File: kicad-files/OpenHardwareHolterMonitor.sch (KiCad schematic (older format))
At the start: 30 parts, among them CON1 Micro_SD_Card, J1 Conn_02x06_Odd_Even, P1 Custom_FTDI, Q1 S8050, Q2 S8050, Q3 Q_NMOS_DGS, Q4 Q_NMOS_DGS, U1 ESP-WROOM-32, Y1 32768Hz

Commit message: continue assigning part numbers for BOM
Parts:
- C1, C2: ManufacturerName (none) -> Yageo; manufacturer-pn C0603C120J5GAC -> CC0603JRNPO9BN120
- CON1: ManufacturerName (none) -> Wurth; manufacturer-pn (none) -> 693072010801
- J1: symbol Connector:Conn_02x06_Odd_Even -> OpenHardwareHolterMonitor-rescue:Conn_02x06_Odd_Even-Connector
- MH_NE1, MH_NW1, MH_SE1, MH_SW1: symbol Mechanical:Mounting_Hole -> OpenHardwareHolterMonitor-rescue:Mounting_Hole-Mechanical
- TP1, TP2, TP3: symbol Connector:Test_Point -> OpenHardwareHolterMonitor-rescue:Test_Point-Connector
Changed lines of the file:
@@
 F 2 "Connectors_Card:MicroSd_Wurth_693072010801" H 3650 5900 50  0001 C CNN
 F 3 "" H 2500 5600 50  0000 C CNN
+F 4 "Wurth" H 0   0   50  0001 C CNN "ManufacturerName"
+F 5 "693072010801" H 0   0   50  0001 C CNN "manufacturer-pn"
 	1    2500 5600
 	0    1    1    0
@@
 F 2 "Capacitors_SMD:C_0603_HandSoldering" H 7988 2600 50  0001 C CNN
 F 3 "" H 7950 2750 50  0000 C CNN
-F 4 "C0603C120J5GAC" H 0   0   50  0001 C CNN "manufacturer-pn"
+F 4 "CC0603JRNPO9BN120 " H 0   0   50  0001 C CNN "manufacturer-pn"
+F 5 "Yageo" H 0   0   50  0001 C CNN "ManufacturerName"
 	1    7950 2750
 	1    0    0    -1
@@
 F 2 "Capacitors_SMD:C_0603_HandSoldering" H 8588 2600 50  0001 C CNN
 F 3 "" H 8550 2750 50  0000 C CNN
-F 4 "C0603C120J5GAC" H 0   0   50  0001 C CNN "manufacturer-pn"
+F 4 "CC0603JRNPO9BN120 " H 0   0   50  0001 C CNN "manufacturer-pn"
+F 5 "Yageo" H 0   0   50  0001 C CNN "ManufacturerName"
 	1    8550 2750
 	1    0    0    -1
@@
 	9550 5600 10200 5600
 $Comp
-L Connector:Test_Point TP1
+L OpenHardwareHolterMonitor-rescue:Test_Point-Connector TP1
 U 1 1 5C99AAF0
 P 10200 5600
@@
 $EndComp
 $Comp
-L Connector:Test_Point TP2
+L OpenHardwareHolterMonitor-rescue:Test_Point-Connector TP2
 U 1 1 5C99ABBF
 P 10200 5800
@@
 $EndComp
 $Comp
-L Connector:Test_Point TP3
+L OpenHardwareHolterMonitor-rescue:Test_Point-Connector TP3
 U 1 1 5C99AC98
 P 10200 6000
@@
 $EndComp
 $Comp
-L Connector:Conn_02x06_Odd_Even J1
+L OpenHardwareHolterMonitor-rescue:Conn_02x06_Odd_Even-Connector J1
 U 1 1 5CAE7D82
 P 10400 2300
@@
 	1350 1900 900  1900
 $Comp
-L Mechanical:Mounting_Hole MH_NW1
+L OpenHardwareHolterMonitor-rescue:Mounting_Hole-Mechanical MH_NW1
 U 1 1 5C1F5248
 P 850 7150
@@
 $EndComp
 $Comp
-L Mechanical:Mounting_Hole MH_SW1
+L OpenHardwareHolterMonitor-rescue:Mounting_Hole-Mechanical MH_SW1
 U 1 1 5C1F5695
 P 850 7450
@@
 $EndComp
 $Comp
-L Mechanical:Mounting_Hole MH_NE1
+L OpenHardwareHolterMonitor-rescue:Mounting_Hole-Mechanical MH_NE1
 U 1 1 5C1F5739
 P 2000 7150
@@
 $EndComp
 $Comp
-L Mechanical:Mounting_Hole MH_SE1
+L OpenHardwareHolterMonitor-rescue:Mounting_Hole-Mechanical MH_SE1
 U 1 1 5C1F57DC
 P 2000 7450

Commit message: someone set us up the BoM
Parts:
- J1: ManufacturerName (none) -> Harwin; manufacturer-pn (none) -> M50-3000645
- P1: ManufacturerName (none) -> Wurth; manufacturer-pn (none) -> 61300711121
- Q1, Q2: ManufacturerName (none) -> Diodes Incorporated; manufacturer-pn (none) -> DSS4240T-7
- Q3, Q4: ManufacturerName (none) -> Diodes Incorporated; manufacturer-pn (none) -> 2N7002-7-F
- R1, R2, R3, R4: ManufacturerName (none) -> Panasonic Electronic Components; manufacturer-pn (none) -> ERA-3AEB470V
- R10, R7: ManufacturerName (none) -> Panasonic Electronic Components; manufacturer-pn (none) -> ERA-3AEB104V
- R11, R8: ManufacturerName (none) -> Panasonic Electronic Components; manufacturer-pn (none) -> ERJ-PB3B3901V
- R12, R9: ManufacturerName (none) -> Panasonic Electronic Components; manufacturer-pn (none) -> ERJ-PB3B1001V
- R5, R6: ManufacturerName (none) -> Panasonic Electronic Components; manufacturer-pn (none) -> ERJ-PB3B1202V
- U1: ManufacturerName (none) -> RF Solutions; manufacturer-pn (none) -> ESP-32
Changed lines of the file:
@@
 F 2 "esp-wroom-32:MODULE_ESP-WROOM-32" H 2550 2550 60  0001 C CNN
 F 3 "" H 2550 2550 60  0001 C CNN
+F 4 " RF Solutions" H 0   0   50  0001 C CNN "ManufacturerName"
+F 5 "ESP-32" H 0   0   50  0001 C CNN "manufacturer-pn"
 	1    2550 2550
 	1    0    0    -1
@@
 F 2 "TO_SOT_Packages_SMD:SOT-23_Handsoldering" H 4900 4975 50  0000 L CIN
 F 3 "" H 4700 5050 50  0000 L CNN
+F 4 "Diodes Incorporated" H 0   0   50  0001 C CNN "ManufacturerName"
+F 5 "DSS4240T-7" H 0   0   50  0001 C CNN "manufacturer-pn"
 	1    4700 5050
 	1    0    0    -1
@@
 F 2 "TO_SOT_Packages_SMD:SOT-23_Handsoldering" H 4900 5725 50  0000 L CIN
 F 3 "" H 4700 5800 50  0000 L CNN
+F 4 "Diodes Incorporated" H 0   0   50  0001 C CNN "ManufacturerName"
+F 5 "DSS4240T-7" H 0   0   50  0001 C CNN "manufacturer-pn"
 	1    4700 5800
 	1    0    0    1
@@
 F 2 "Resistors_SMD:R_0603_HandSoldering" V 4180 5050 50  0001 C CNN
 F 3 "" H 4250 5050 50  0000 C CNN
+F 4 "Panasonic Electronic Components" H 0   0   50  0001 C CNN "ManufacturerName"
+F 5 "ERJ-PB3B1202V" H 0   0   50  0001 C CNN "manufacturer-pn"
 	1    4250 5050
 	0    1    1    0
@@
 F 2 "Resistors_SMD:R_0603_HandSoldering" V 4180 5800 50  0001 C CNN
 F 3 "" H 4250 5800 50  0000 C CNN
+F 4 "Panasonic Electronic Components" H 0   0   50  0001 C CNN "ManufacturerName"
+F 5 "ERJ-PB3B1202V" H 0   0   50  0001 C CNN "manufacturer-pn"
 	1    4250 5800
 	0    1    1    0
@@
 F 2 "Pin_Headers:Pin_Header_Straight_1x07_Pitch2.54mm" H 5300 6650 50  0001 C CNN
 F 3 "" H 5300 6650 50  0000 C CNN
+F 4 "Wurth" H 0   0   50  0001 C CNN "ManufacturerName"
+F 5 "61300711121" H 0   0   50  0001 C CNN "manufacturer-pn"
 	1    5300 6650
 	1    0    0    -1
@@
 F 2 "Resistors_SMD:R_0603_HandSoldering" V 4280 2000 50  0001 C CNN
 F 3 "" H 4350 2000 50  0000 C CNN
+F 4 "Panasonic Electronic Components" H 0   0   50  0001 C CNN "ManufacturerName"
+F 5 "ERA-3AEB470V" H 0   0   50  0001 C CNN "manufacturer-pn"
 	1    4350 2000
 	0    1    1    0
@@
 F 2 "Resistors_SMD:R_0603_HandSoldering" V 4280 2700 50  0001 C CNN
 F 3 "" H 4350 2700 50  0000 C CNN
+F 4 "Panasonic Electronic Components" H 0   0   50  0001 C CNN "ManufacturerName"
+F 5 "ERA-3AEB470V" H 0   0   50  0001 C CNN "manufacturer-pn"
 	1    4350 2700
 	0    1    1    0
@@
 F 2 "Resistors_SMD:R_0603_HandSoldering" V 4280 2800 50  0001 C CNN
 F 3 "" H 4350 2800 50  0000 C CNN
+F 4 "Panasonic Electronic Components" H 0   0   50  0001 C CNN "ManufacturerName"
+F 5 "ERA-3AEB470V" H 0   0   50  0001 C CNN "manufacturer-pn"
 	1    4350 2800
 	0    1    1    0
@@
 F 2 "Resistors_SMD:R_0603_HandSoldering" V 4280 2900 50  0001 C CNN
 F 3 "" H 4350 2900 50  0000 C CNN
+F 4 "Panasonic Electronic Components" H 0   0   50  0001 C CNN "ManufacturerName"
+F 5 "ERA-3AEB470V" H 0   0   50  0001 C CNN "manufacturer-pn"
 	1    4350 2900
 	0    1    1    0
@@
 F 2 "Resistors_SMD:R_0603_HandSoldering" V 8380 3950 50  0001 C CNN
 F 3 "" H 8450 3950 50  0000 C CNN
+F 4 "Panasonic Electronic Components" H 0   0   50  0001 C CNN "ManufacturerName"
+F 5 "ERJ-PB3B3901V" H 0   0   50  0001 C CNN "manufacturer-pn"
 	1    8450 3950
 	1    0    0    -1
@@
 F 2 "Resistors_SMD:R_0603_HandSoldering" V 8380 4400 50  0001 C CNN
 F 3 "" H 8450 4400 50  0000 C CNN
+F 4 "Panasonic Electronic Components" H 0   0   50  0001 C CNN "ManufacturerName"
+F 5 "ERJ-PB3B1001V" H 0   0   50  0001 C CNN "manufacturer-pn"
 	1    8450 4400
 	1    0    0    -1
@@
 F 2 "TO_SOT_Packages_SMD:SOT-23W_Handsoldering" H 8550 4900 50  0001 C CNN
 F 3 "" H 8350 4800 50  0000 C CNN
+F 4 "Diodes Incorporated" H 0   0   50  0001 C CNN "ManufacturerName"
+F 5 "2N7002-7-F " H 0   0   50  0001 C CNN "manufacturer-pn"
 	1    8350 4800
 	1    0    0    -1
@@
 F 2 "Resistors_SMD:R_0603_HandSoldering" V 10130 3950 50  0001 C CNN
 F 3 "" H 10200 3950 50  0000 C CNN
+F 4 "Panasonic Electronic Components" H 0   0   50  0001 C CNN "ManufacturerName"
+F 5 "ERJ-PB3B3901V" H 0   0   50  0001 C CNN "manufacturer-pn"
 	1    10200 3950
 	1    0    0    -1
@@
 F 2 "Resistors_SMD:R_0603_HandSoldering" V 10130 4400 50  0001 C CNN
 F 3 "" H 10200 4400 50  0000 C CNN
+F 4 "Panasonic Electronic Components" H 0   0   50  0001 C CNN "ManufacturerName"
+F 5 "ERJ-PB3B1001V" H 0   0   50  0001 C CNN "manufacturer-pn"
 	1    10200 4400
 	1    0    0    -1
@@
 F 2 "TO_SOT_Packages_SMD:SOT-23W_Handsoldering" H 10300 4900 50  0001 C CNN
 F 3 "" H 10100 4800 50  0000 C CNN
+F 4 "Diodes Incorporated" H 0   0   50  0001 C CNN "ManufacturerName"
+F 5 "2N7002-7-F " H 0   0   50  0001 C CNN "manufacturer-pn"
 	1    10100 4800
 	1    0    0    -1
@@
 F 2 "Resistors_SMD:R_0603_HandSoldering" V 9580 5000 50  0001 C CNN
 F 3 "" H 9650 5000 50  0000 C CNN
+F 4 "Panasonic Electronic Components" H 0   0   50  0001 C CNN "ManufacturerName"
+F 5 "ERA-3AEB104V" H 0   0   50  0001 C CNN "manufacturer-pn"
 	1    9650 5000
 	1    0    0    -1
@@
 F 2 "Resistors_SMD:R_0603_HandSoldering" V 7830 5000 50  0001 C CNN
 F 3 "" H 7900 5000 50  0000 C CNN
+F 4 "Panasonic Electronic Components" H 0   0   50  0001 C CNN "ManufacturerName"
+F 5 "ERA-3AEB104V" H 0   0   50  0001 C CNN "manufacturer-pn"
 	1    7900 5000
 	1    0    0    -1
@@
 F 2 "Pin_Headers:Pin_Header_Straight_2x06_Pitch1.27mm" H 10400 2300 50  0001 C CNN
 F 3 "~" H 10400 2300 50  0001 C CNN
+F 4 "Harwin" H 0   0   50  0001 C CNN "ManufacturerName"
+F 5 "M50-3000645" H 0   0   50  0001 C CNN "manufacturer-pn"
 	1    10400 2300
 	1    0    0    -1

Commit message: checked BoM
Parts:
- Y1: ManufacturerName (none) -> Fox
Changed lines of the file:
@@
 F 3 "" H 8250 2300 50  0000 C CNN
 F 4 "FK161EIHM0.032768" H 8250 2150 50  0000 C CNN "manufacturer-pn"
+F 5 "Fox" H 0   0   50  0001 C CNN "ManufacturerName"
 	1    8250 2300
 	1    0    0    -1

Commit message: fix schematic to use standard transistor pin numbers
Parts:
- Q1, Q2: symbol OpenHardwareHolterMonitor-rescue:S8050 -> Device:Q_NPN_BEC
- Q3, Q4: value Q_NMOS_DGS -> 2N7002; symbol OpenHardwareHolterMonitor-rescue:Q_NMOS_DGS -> Device:Q_NMOS_GSD
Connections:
- net DTR: now also Q2.2 (E); no longer Q2.1 (E)
- net Enable_vbat_read: now also Q3.1 (G), Q4.1 (G); no longer Q3.2 (G), Q4.2 (G)
- net GND: now also Q3.2 (S), Q4.2 (S); no longer Q3.3 (S), Q4.3 (S)
- net RTS: now also Q1.2 (E); no longer Q1.1 (E)
- net at R5.1: now also Q1.1 (B); no longer Q1.2 (B)
- net at R6.1: now also Q2.1 (B); no longer Q2.2 (B)
- net at R9.2: now also Q3.3 (D); no longer Q3.1 (D)
- net at R12.2: now also Q4.3 (D); no longer Q4.1 (D)
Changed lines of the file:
@@
 $EndComp
 $Comp
-L OpenHardwareHolterMonitor-rescue:S8050 Q1
+L Device:Q_NPN_BEC Q1
 U 1 1 5A2C0790
 P 4700 5050
@@
 $EndComp
 $Comp
-L OpenHardwareHolterMonitor-rescue:S8050 Q2
+L Device:Q_NPN_BEC Q2
 U 1 1 5A2C0855
 P 4700 5800
@@
 	8450 3750 8450 3800
 $Comp
-L OpenHardwareHolterMonitor-rescue:Q_NMOS_DGS Q3
+L Device:Q_NMOS_GSD Q3
 U 1 1 5AB6876E
 P 8350 4800
 F 0 "Q3" H 8550 4850 50  0000 L CNN
-F 1 "Q_NMOS_DGS" H 8550 4750 50  0000 L CNN
+F 1 "2N7002" H 8550 4750 50  0000 L CNN
 F 2 "TO_SOT_Packages_SMD:SOT-23W_Handsoldering" H 8550 4900 50  0001 C CNN
 F 3 "" H 8350 4800 50  0000 C CNN
@@
 	10200 3750 10200 3800
 $Comp
-L OpenHardwareHolterMonitor-rescue:Q_NMOS_DGS Q4
+L Device:Q_NMOS_GSD Q4
 U 1 1 5AB6D189
 P 10100 4800
 F 0 "Q4" H 10300 4850 50  0000 L CNN
-F 1 "Q_NMOS_DGS" H 10300 4750 50  0000 L CNN
+F 1 "2N7002" H 10300 4750 50  0000 L CNN
 F 2 "TO_SOT_Packages_SMD:SOT-23W_Handsoldering" H 10300 4900 50  0001 C CNN
 F 3 "" H 10100 4800 50  0000 C CNN

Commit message: switch to consistent SOT-23 footprint
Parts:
- Q3, Q4: footprint TO_SOT_Packages_SMD:SOT-23W_Handsoldering -> TO_SOT_Packages_SMD:SOT-23_Handsoldering
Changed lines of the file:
@@
 F 0 "Q3" H 8550 4850 50  0000 L CNN
 F 1 "2N7002" H 8550 4750 50  0000 L CNN
-F 2 "TO_SOT_Packages_SMD:SOT-23W_Handsoldering" H 8550 4900 50  0001 C CNN
+F 2 "TO_SOT_Packages_SMD:SOT-23_Handsoldering" H 8550 4900 50  0001 C CNN
 F 3 "" H 8350 4800 50  0000 C CNN
 F 4 "Diodes Incorporated" H 0   0   50  0001 C CNN "ManufacturerName"
@@
 F 0 "Q4" H 10300 4850 50  0000 L CNN
 F 1 "2N7002" H 10300 4750 50  0000 L CNN
-F 2 "TO_SOT_Packages_SMD:SOT-23W_Handsoldering" H 10300 4900 50  0001 C CNN
+F 2 "TO_SOT_Packages_SMD:SOT-23_Handsoldering" H 10300 4900 50  0001 C CNN
 F 3 "" H 10100 4800 50  0000 C CNN
 F 4 "Diodes Incorporated" H 0   0   50  0001 C CNN "ManufacturerName"

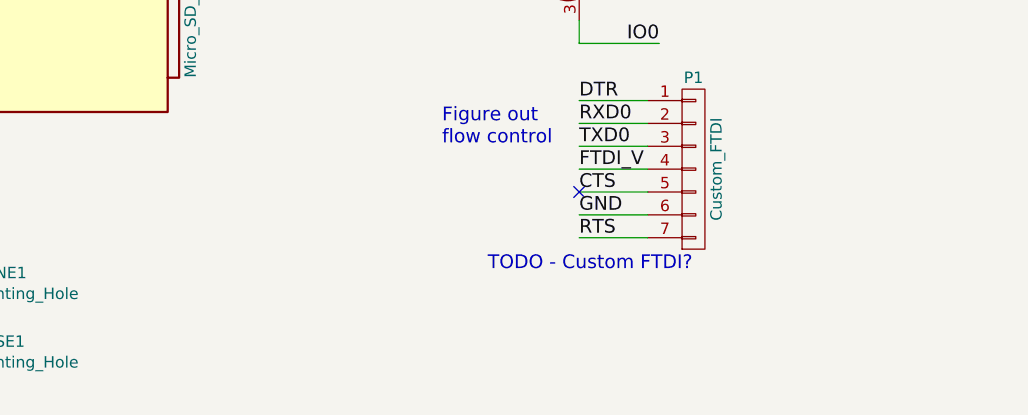
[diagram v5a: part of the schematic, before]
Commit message: Align Fiducials and Logo on schematic and PCB
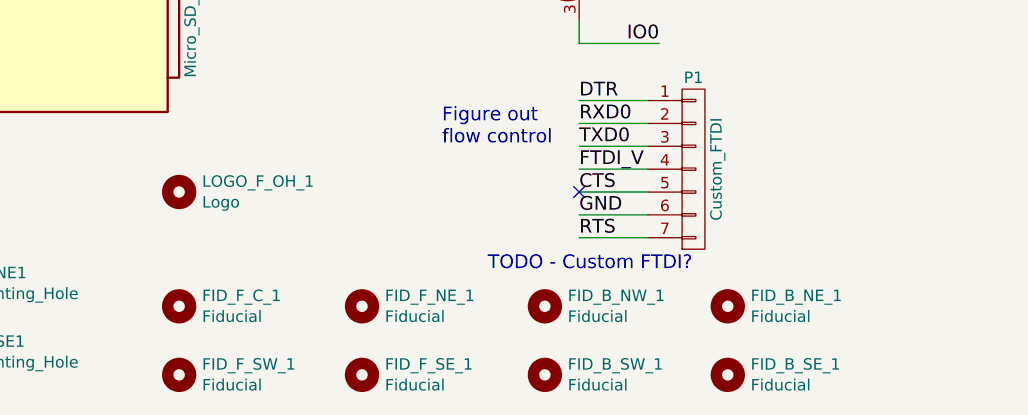
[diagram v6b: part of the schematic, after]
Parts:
- added FID_B_NE_1, FID_B_NW_1, FID_B_SE_1, FID_B_SW_1, FID_F_C_1, FID_F_NE_1, FID_F_SE_1, FID_F_SW_1: Fiducial, Fiducial:Fiducial_1mm_Dia_2.54mm_Outer_CopperTop, symbol OpenHardwareHolterMonitor-rescue:Mounting_Hole-Mechanical
- added LOGO_F_OH_1: Logo, Symbol:OSHW-Logo2_9.8x8mm_SilkScreen, symbol OpenHardwareHolterMonitor-rescue:Mounting_Hole-Mechanical
- R1, R10, R11, R12, R2, R3, R4, R5, R6, R7, R8, R9: footprint Resistors_SMD:R_0603_HandSoldering -> Resistor_SMD:R_0603_1608Metric_Pad1.05x0.95mm_HandSolder
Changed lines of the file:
@@
 F 0 "R5" V 4330 5050 50  0000 C CNN
 F 1 "12K" V 4250 5050 50  0000 C CNN
-F 2 "Resistors_SMD:R_0603_HandSoldering" V 4180 5050 50  0001 C CNN
+F 2 "Resistor_SMD:R_0603_1608Metric_Pad1.05x0.95mm_HandSolder" V 4180 5050 50  0001 C CNN
 F 3 "" H 4250 5050 50  0000 C CNN
 F 4 "Panasonic Electronic Components" H 0   0   50  0001 C CNN "ManufacturerName"
@@
 F 0 "R6" V 4330 5800 50  0000 C CNN
 F 1 "12K" V 4250 5800 50  0000 C CNN
-F 2 "Resistors_SMD:R_0603_HandSoldering" V 4180 5800 50  0001 C CNN
+F 2 "Resistor_SMD:R_0603_1608Metric_Pad1.05x0.95mm_HandSolder" V 4180 5800 50  0001 C CNN
 F 3 "" H 4250 5800 50  0000 C CNN
 F 4 "Panasonic Electronic Components" H 0   0   50  0001 C CNN "ManufacturerName"
@@
 F 0 "R1" V 4430 2000 50  0000 C CNN
 F 1 "47" V 4350 2000 50  0000 C CNN
-F 2 "Resistors_SMD:R_0603_HandSoldering" V 4280 2000 50  0001 C CNN
+F 2 "Resistor_SMD:R_0603_1608Metric_Pad1.05x0.95mm_HandSolder" V 4280 2000 50  0001 C CNN
 F 3 "" H 4350 2000 50  0000 C CNN
 F 4 "Panasonic Electronic Components" H 0   0   50  0001 C CNN "ManufacturerName"
@@
 F 0 "R2" V 4430 2700 50  0000 C CNN
 F 1 "47" V 4350 2700 50  0000 C CNN
-F 2 "Resistors_SMD:R_0603_HandSoldering" V 4280 2700 50  0001 C CNN
+F 2 "Resistor_SMD:R_0603_1608Metric_Pad1.05x0.95mm_HandSolder" V 4280 2700 50  0001 C CNN
 F 3 "" H 4350 2700 50  0000 C CNN
 F 4 "Panasonic Electronic Components" H 0   0   50  0001 C CNN "ManufacturerName"
@@
 F 0 "R3" V 4430 2800 50  0000 C CNN
 F 1 "47" V 4350 2800 50  0000 C CNN
-F 2 "Resistors_SMD:R_0603_HandSoldering" V 4280 2800 50  0001 C CNN
+F 2 "Resistor_SMD:R_0603_1608Metric_Pad1.05x0.95mm_HandSolder" V 4280 2800 50  0001 C CNN
 F 3 "" H 4350 2800 50  0000 C CNN
 F 4 "Panasonic Electronic Components" H 0   0   50  0001 C CNN "ManufacturerName"
@@
 F 0 "R4" V 4430 2900 50  0000 C CNN
 F 1 "47" V 4350 2900 50  0000 C CNN
-F 2 "Resistors_SMD:R_0603_HandSoldering" V 4280 2900 50  0001 C CNN
+F 2 "Resistor_SMD:R_0603_1608Metric_Pad1.05x0.95mm_HandSolder" V 4280 2900 50  0001 C CNN
 F 3 "" H 4350 2900 50  0000 C CNN
 F 4 "Panasonic Electronic Components" H 0   0   50  0001 C CNN "ManufacturerName"
@@
 F 0 "R8" V 8530 3950 50  0000 C CNN
 F 1 "3.9k" V 8450 3950 50  0000 C CNN
-F 2 "Resistors_SMD:R_0603_HandSoldering" V 8380 3950 50  0001 C CNN
+F 2 "Resistor_SMD:R_0603_1608Metric_Pad1.05x0.95mm_HandSolder" V 8380 3950 50  0001 C CNN
 F 3 "" H 8450 3950 50  0000 C CNN
 F 4 "Panasonic Electronic Components" H 0   0   50  0001 C CNN "ManufacturerName"
@@
 F 0 "R9" V 8530 4400 50  0000 C CNN
 F 1 "1k" V 8450 4400 50  0000 C CNN
-F 2 "Resistors_SMD:R_0603_HandSoldering" V 8380 4400 50  0001 C CNN
+F 2 "Resistor_SMD:R_0603_1608Metric_Pad1.05x0.95mm_HandSolder" V 8380 4400 50  0001 C CNN
 F 3 "" H 8450 4400 50  0000 C CNN
 F 4 "Panasonic Electronic Components" H 0   0   50  0001 C CNN "ManufacturerName"
@@
 F 0 "R11" V 10280 3950 50  0000 C CNN
 F 1 "3.9k" V 10200 3950 50  0000 C CNN
-F 2 "Resistors_SMD:R_0603_HandSoldering" V 10130 3950 50  0001 C CNN
+F 2 "Resistor_SMD:R_0603_1608Metric_Pad1.05x0.95mm_HandSolder" V 10130 3950 50  0001 C CNN
 F 3 "" H 10200 3950 50  0000 C CNN
 F 4 "Panasonic Electronic Components" H 0   0   50  0001 C CNN "ManufacturerName"
@@
 F 0 "R12" V 10280 4400 50  0000 C CNN
 F 1 "1k" V 10200 4400 50  0000 C CNN
-F 2 "Resistors_SMD:R_0603_HandSoldering" V 10130 4400 50  0001 C CNN
+F 2 "Resistor_SMD:R_0603_1608Metric_Pad1.05x0.95mm_HandSolder" V 10130 4400 50  0001 C CNN
 F 3 "" H 10200 4400 50  0000 C CNN
 F 4 "Panasonic Electronic Components" H 0   0   50  0001 C CNN "ManufacturerName"
@@
 F 0 "R10" V 9730 5000 50  0000 C CNN
 F 1 "100k" V 9650 5000 50  0000 C CNN
-F 2 "Resistors_SMD:R_0603_HandSoldering" V 9580 5000 50  0001 C CNN
+F 2 "Resistor_SMD:R_0603_1608Metric_Pad1.05x0.95mm_HandSolder" V 9580 5000 50  0001 C CNN
 F 3 "" H 9650 5000 50  0000 C CNN
 F 4 "Panasonic Electronic Components" H 0   0   50  0001 C CNN "ManufacturerName"
@@
 F 0 "R7" V 7980 5000 50  0000 C CNN
 F 1 "100k" V 7900 5000 50  0000 C CNN
-F 2 "Resistors_SMD:R_0603_HandSoldering" V 7830 5000 50  0001 C CNN
+F 2 "Resistor_SMD:R_0603_1608Metric_Pad1.05x0.95mm_HandSolder" V 7830 5000 50  0001 C CNN
 F 3 "" H 7900 5000 50  0000 C CNN
 F 4 "Panasonic Electronic Components" H 0   0   50  0001 C CNN "ManufacturerName"
@@
 	1    0    0    -1
 $EndComp
+$Comp
+L OpenHardwareHolterMonitor-rescue:Mounting_Hole-Mechanical FID_F_C_1
+U 1 1 5D2AFEF5
+P 3050 7250
+F 0 "FID_F_C_1" H 3150 7296 50  0000 L CNN
+F 1 "Fiducial" H 3150 7205 50  0000 L CNN
+F 2 "Fiducial:Fiducial_1mm_Dia_2.54mm_Outer_CopperTop" H 3050 7250 50  0001 C CNN
+F 3 "" H 3050 7250 50  0001 C CNN
+	1    3050 7250
+	1    0    0    -1
+$EndComp
+$Comp
+L OpenHardwareHolterMonitor-rescue:Mounting_Hole-Mechanical FID_F_SW_1
+U 1 1 5D2AFEFC
+P 3050 7550
+F 0 "FID_F_SW_1" H 3150 7596 50  0000 L CNN
+F 1 "Fiducial" H 3150 7505 50  0000 L CNN
+F 2 "Fiducial:Fiducial_1mm_Dia_2.54mm_Outer_CopperTop" H 3050 7550 50  0001 C CNN
+F 3 "" H 3050 7550 50  0001 C CNN
+	1    3050 7550
+	1    0    0    -1
+$EndComp
+$Comp
+L OpenHardwareHolterMonitor-rescue:Mounting_Hole-Mechanical FID_F_NE_1
+U 1 1 5D2AFF03
+P 3850 7250
+F 0 "FID_F_NE_1" H 3950 7296 50  0000 L CNN
+F 1 "Fiducial" H 3950 7205 50  0000 L CNN
+F 2 "Fiducial:Fiducial_1mm_Dia_2.54mm_Outer_CopperTop" H 3850 7250 50  0001 C CNN
+F 3 "" H 3850 7250 50  0001 C CNN
+	1    3850 7250
+	1    0    0    -1
+$EndComp
+$Comp
+L OpenHardwareHolterMonitor-rescue:Mounting_Hole-Mechanical FID_F_SE_1
+U 1 1 5D2AFF0A
+P 3850 7550
+F 0 "FID_F_SE_1" H 3950 7596 50  0000 L CNN
+F 1 "Fiducial" H 3950 7505 50  0000 L CNN
+F 2 "Fiducial:Fiducial_1mm_Dia_2.54mm_Outer_CopperTop" H 3850 7550 50  0001 C CNN
+F 3 "" H 3850 7550 50  0001 C CNN
+	1    3850 7550
+	1    0    0    -1
+$EndComp
+$Comp
+L OpenHardwareHolterMonitor-rescue:Mounting_Hole-Mechanical FID_B_NW_1
+U 1 1 5D2C0C22
+P 4650 7250
+F 0 "FID_B_NW_1" H 4750 7296 50  0000 L CNN
+F 1 "Fiducial" H 4750 7205 50  0000 L CNN
+F 2 "Fiducial:Fiducial_1mm_Dia_2.54mm_Outer_CopperTop" H 4650 7250 50  0001 C CNN
+F 3 "" H 4650 7250 50  0001 C CNN
+	1    4650 7250
+	1    0    0    -1
+$EndComp
+$Comp
+L OpenHardwareHolterMonitor-rescue:Mounting_Hole-Mechanical FID_B_SW_1
+U 1 1 5D2C0C29
+P 4650 7550
+F 0 "FID_B_SW_1" H 4750 7596 50  0000 L CNN
+F 1 "Fiducial" H 4750 7505 50  0000 L CNN
+F 2 "Fiducial:Fiducial_1mm_Dia_2.54mm_Outer_CopperTop" H 4650 7550 50  0001 C CNN
+F 3 "" H 4650 7550 50  0001 C CNN
+	1    4650 7550
+	1    0    0    -1
+$EndComp
+$Comp
+L OpenHardwareHolterMonitor-rescue:Mounting_Hole-Mechanical FID_B_NE_1
+U 1 1 5D2C0C30
+P 5450 7250
+F 0 "FID_B_NE_1" H 5550 7296 50  0000 L CNN
+F 1 "Fiducial" H 5550 7205 50  0000 L CNN
+F 2 "Fiducial:Fiducial_1mm_Dia_2.54mm_Outer_CopperTop" H 5450 7250 50  0001 C CNN
+F 3 "" H 5450 7250 50  0001 C CNN
+	1    5450 7250
+	1    0    0    -1
+$EndComp
+$Comp
+L OpenHardwareHolterMonitor-rescue:Mounting_Hole-Mechanical FID_B_SE_1
+U 1 1 5D2C0C37
+P 5450 7550
+F 0 "FID_B_SE_1" H 5550 7596 50  0000 L CNN
+F 1 "Fiducial" H 5550 7505 50  0000 L CNN
+F 2 "Fiducial:Fiducial_1mm_Dia_2.54mm_Outer_CopperTop" H 5450 7550 50  0001 C CNN
+F 3 "" H 5450 7550 50  0001 C CNN
+	1    5450 7550
+	1    0    0    -1
+$EndComp
+$Comp
+L OpenHardwareHolterMonitor-rescue:Mounting_Hole-Mechanical LOGO_F_OH_1
+U 1 1 5D2C999A
+P 3050 6750
+F 0 "LOGO_F_OH_1" H 3150 6796 50  0000 L CNN
+F 1 "Logo" H 3150 6705 50  0000 L CNN
+F 2 "Symbol:OSHW-Logo2_9.8x8mm_SilkScreen" H 3050 6750 50  0001 C CNN
+F 3 "" H 3050 6750 50  0001 C CNN
+	1    3050 6750
+	1    0    0    -1
+$EndComp
